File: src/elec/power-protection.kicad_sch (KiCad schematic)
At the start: 11 parts, among them J1 Conn_01x03_Pin, Q1 BSS138, Q2 BSS138, Q3 BC857, Q4 BC857

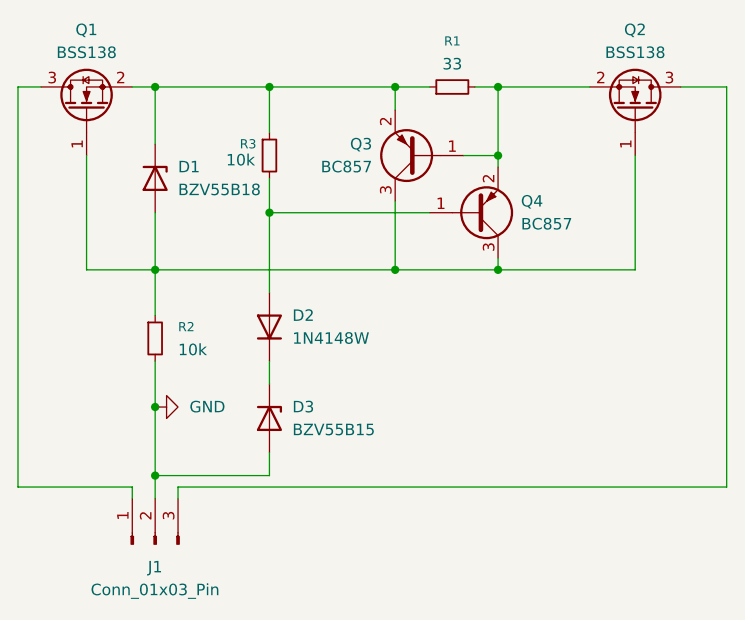
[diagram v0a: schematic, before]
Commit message: Fix: wrong MOSFET (p channel needed); README.md added
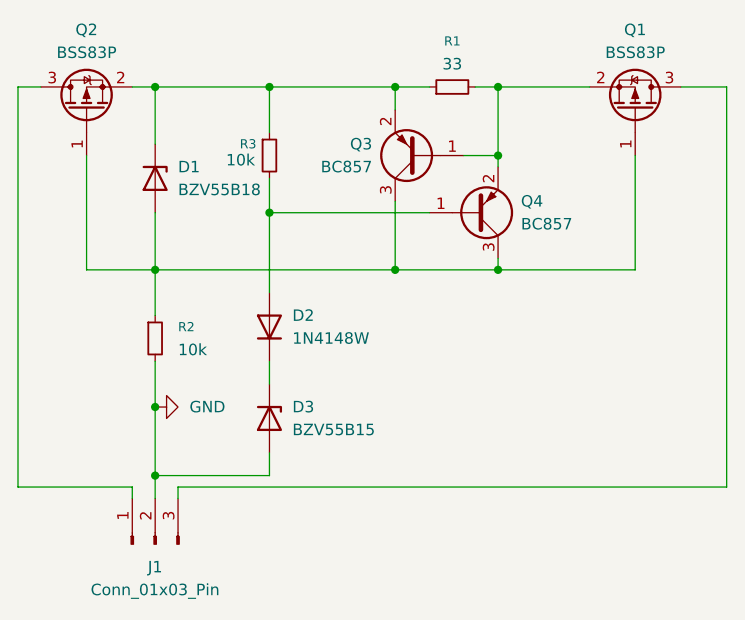
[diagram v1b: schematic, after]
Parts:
- removed Q1, Q2: BSS138, Package_TO_SOT_SMD:SOT-23, symbol Transistor_FET:BSS138
- added Q1, Q2: BSS83P, Package_TO_SOT_SMD:SOT-23, symbol Transistor_FET:BSS83P
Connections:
- net at J1.1 (Pin_1): now also Q2.3 (D)
- net at J1.3 (Pin_3): now also Q1.3 (D)
- net at Q3.1 (B), Q4.2 (E), R1.2: now also Q1.2 (S)
- net at D1.1 (K), Q3.2 (E), R1.1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: now also Q2.2 (S)
- net at D1.2 (A), Q3.3 (C), Q4.3 (C)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: now also Q1.1 (G), Q2.1 (G)
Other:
- title: (none) -> FUSE UIr
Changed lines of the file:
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@@
 	(generator_version "9.0")
 	(paper "A4")
+	(title_block
+		(title "FUSE UIr")
+		(date "2026-01-03")
+		(rev "0.2")
+	)
 	(junction
 		(at 62.23 26.67)
@@
 	)
 	(symbol
+		(lib_id "Transistor_FET:BSS83P")
+		(at 54.61 29.21 90)
+		(unit 1)
+		(exclude_from_sim no)
+		(in_bom yes)
+		(on_board yes)
+		(dnp no)
+		(property "Reference" "Q2"
+			(at 54.61 20.32 90)
+			(effects
+				(font
+					(size 1.27 1.27)
+				)
+			)
+		)
+		(property "Value" "BSS83P"
+			(at 54.61 22.86 90)
+			(effects
+				(font
+					(size 1.27 1.27)
+				)
+			)
+		)
+		(property "Footprint" "Package_TO_SOT_SMD:SOT-23"
+			(at 56.515 24.13 0)
+			(effects
+				(font
+					(size 1.27 1.27)
+					(italic yes)
+				)
+				(justify left)
+				(hide yes)
+			)
+		)
+		(property "Datasheet" "http://www.farnell.com/datasheets/1835997.pdf"
+			(at 58.42 24.13 0)
+			(effects
+				(font
+					(size 1.27 1.27)
+				)
+				(justify left)
+				(hide yes)
+			)
+		)
+		(property "Description" "-0.33A Id, -60V Vds, P-Channel MOSFET, SOT-23"
+			(at 54.61 29.21 0)
+			(effects
+				(font
+					(size 1.27 1.27)
+				)
+				(hide yes)
+			)
+		)
+		(pin "2"
+		)
+		(pin "1"
+		)
+		(pin "3"
+		)
+		(instances
+			(project "power-protection"
+				(path "/f96ba537-a636-4056-ab3e-8435b128c895"
+					(reference "Q2")
+					(unit 1)
+				)
+			)
+		)
+	)
+	(symbol
 		(lib_id "Diode:BZV55B15")
 		(at 74.93 63.5 270)
@@
 	)
 	(symbol
-		(lib_id "Transistor_FET:BSS138")
-		(at 115.57 29.21 270)
-		(mirror x)
-		(unit 1)
-		(exclude_from_sim no)
-		(in_bom yes)
-		(on_board yes)
-		(dnp no)
-		(property "Reference" "Q2"
-			(at 115.57 20.32 90)
-			(effects
-				(font
-					(size 1.27 1.27)
-				)
-			)
-		)
-		(property "Value" "BSS138"
-			(at 115.57 22.86 90)
-			(effects
-				(font
-					(size 1.27 1.27)
-				)
-			)
-		)
-		(property "Footprint" "Package_TO_SOT_SMD:SOT-23"
-			(at 113.665 24.13 0)
-			(effects
-				(font
-					(size 1.27 1.27)
-					(italic yes)
-				)
-				(justify left)
-				(hide yes)
-			)
-		)
-		(property "Datasheet" "https://www.onsemi.com/pub/Collateral/BSS138-D.PDF"
-			(at 111.76 24.13 0)
-			(effects
-				(font
-					(size 1.27 1.27)
-				)
-				(justify left)
-				(hide yes)
-			)
-		)
-		(property "Description" "50V Vds, 0.22A Id, N-Channel MOSFET, SOT-23"
-			(at 115.57 29.21 0)
-			(effects
-				(font
-					(size 1.27 1.27)
-				)
-				(hide yes)
-			)
-		)
-		(pin "2"
-		)
-		(pin "3"
-		)
-		(pin "1"
-		)
-		(instances
-			(project ""
-				(path "/f96ba537-a636-4056-ab3e-8435b128c895"
-					(reference "Q2")
-					(unit 1)
-				)
-			)
-		)
-	)
-	(symbol
 		(lib_id "Device:R_Small")
 		(at 74.93 34.29 0)
@@
 	)
 	(symbol
-		(lib_id "Transistor_FET:BSS138")
-		(at 54.61 29.21 90)
+		(lib_id "Transistor_FET:BSS83P")
+		(at 115.57 29.21 270)
+		(mirror x)
 		(unit 1)
 		(exclude_from_sim no)
@@
 		(on_board yes)
 		(dnp no)
-		(fields_autoplaced yes)
 		(property "Reference" "Q1"
-			(at 54.61 20.32 90)
-			(effects
-				(font
-					(size 1.27 1.27)
-				)
-			)
-		)
-		(property "Value" "BSS138"
-			(at 54.61 22.86 90)
+			(at 115.57 20.32 90)
+			(effects
+				(font
+					(size 1.27 1.27)
+				)
+			)
+		)
+		(property "Value" "BSS83P"
+			(at 115.57 22.86 90)
 			(effects
 				(font
@@
 		)
 		(property "Footprint" "Package_TO_SOT_SMD:SOT-23"
-			(at 56.515 24.13 0)
+			(at 113.665 24.13 0)
 			(effects
 				(font
@@
 			)
 		)
-		(property "Datasheet" "https://www.onsemi.com/pub/Collateral/BSS138-D.PDF"
-			(at 58.42 24.13 0)
-			(effects
-				(font
-					(size 1.27 1.27)
-				)
-				(justify left)
-				(hide yes)
-			)
-		)
-		(property "Description" "50V Vds, 0.22A Id, N-Channel MOSFET, SOT-23"
-			(at 54.61 29.21 0)
+		(property "Datasheet" "http://www.farnell.com/datasheets/1835997.pdf"
+			(at 111.76 24.13 0)
+			(effects
+				(font
+					(size 1.27 1.27)
+				)
+				(justify left)
+				(hide yes)
+			)
+		)
+		(property "Description" "-0.33A Id, -60V Vds, P-Channel MOSFET, SOT-23"
+			(at 115.57 29.21 0)
 			(effects
 				(font
@@
 		(pin "2"
 		)
+		(pin "1"
+		)
 		(pin "3"
 		)
-		(pin "1"
-		)
 		(instances
-			(project ""
+			(project "power-protection"
 				(path "/f96ba537-a636-4056-ab3e-8435b128c895"
 					(reference "Q1")

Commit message: started fixing
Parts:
- removed D2: 1N4148W, Diode_SMD:D_SOD-123, symbol Diode:1N4148W
- added R4: 10k, Resistor_SMD:R_0805_2012Metric, symbol Device:R_Small
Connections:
- net at D3.1 (K): now also R3.2, R4.2
- net at Q4.1 (B): now also R4.1; no longer R3.2
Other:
- moved on the sheet: D3
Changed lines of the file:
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@@
+	)
+	(junction
+		(at 62.23 68.58)
+		(diameter 0)
+		(color 0 0 0 0)
 	)
 	(junction
@@
 	)
 	(junction
-		(at 62.23 62.23)
-		(diameter 0)
-		(color 0 0 0 0)
-	)
-	(junction
-		(at 62.23 69.85)
-		(diameter 0)
-		(color 0 0 0 0)
-	)
-	(junction
 		(at 100.33 26.67)
 		(diameter 0)
@@
 	)
 	(junction
+		(at 62.23 59.69)
+		(diameter 0)
+		(color 0 0 0 0)
+	)
+	(junction
 		(at 100.33 34.29)
 		(diameter 0)
@@
 	(wire
 		(pts
-			(xy 74.93 67.31) (xy 74.93 69.85)
+			(xy 74.93 58.42) (xy 74.93 59.69)
 		)
 		(stroke
@@
 	(wire
 		(pts
+			(xy 76.2 40.64) (xy 74.93 40.64)
+		)
+		(stroke
+			(width 0)
+			(type default)
+		)
+	)
+	(wire
+		(pts
 			(xy 125.73 71.12) (xy 64.77 71.12)
 		)
@@
 	(wire
 		(pts
-			(xy 62.23 62.23) (xy 62.23 69.85)
-		)
-		(stroke
-			(width 0)
-			(type default)
-		)
-	)
-	(wire
-		(pts
 			(xy 62.23 26.67) (xy 62.23 33.02)
 		)
@@
 	(wire
 		(pts
-			(xy 62.23 69.85) (xy 74.93 69.85)
+			(xy 62.23 59.69) (xy 74.93 59.69)
 		)
 		(stroke
@@
 	(wire
 		(pts
-			(xy 74.93 40.64) (xy 74.93 49.53)
-		)
-		(stroke
-			(width 0)
-			(type default)
-		)
-	)
-	(wire
-		(pts
 			(xy 100.33 45.72) (xy 100.33 46.99)
 		)
@@
 	(wire
 		(pts
-			(xy 62.23 69.85) (xy 62.23 72.39)
-		)
-		(stroke
-			(width 0)
-			(type default)
-		)
-	)
-	(wire
-		(pts
-			(xy 92.71 40.64) (xy 74.93 40.64)
+			(xy 62.23 59.69) (xy 62.23 68.58)
+		)
+		(stroke
+			(width 0)
+			(type default)
+		)
+	)
+	(wire
+		(pts
+			(xy 92.71 40.64) (xy 81.28 40.64)
 		)
 		(stroke
@@
 	(wire
 		(pts
-			(xy 62.23 57.15) (xy 62.23 62.23)
+			(xy 62.23 57.15) (xy 62.23 59.69)
 		)
 		(stroke
@@
 	(wire
 		(pts
+			(xy 62.23 68.58) (xy 62.23 72.39)
+		)
+		(stroke
+			(width 0)
+			(type default)
+		)
+	)
+	(wire
+		(pts
 			(xy 100.33 34.29) (xy 100.33 35.56)
 		)
@@
 	(wire
 		(pts
-			(xy 74.93 57.15) (xy 74.93 59.69)
+			(xy 74.93 40.64) (xy 74.93 50.8)
 		)
 		(stroke
@@
 	(symbol
 		(lib_id "Diode:BZV55B15")
-		(at 74.93 63.5 270)
+		(at 74.93 54.61 270)
 		(unit 1)
 		(exclude_from_sim no)
@@
 		(fields_autoplaced yes)
 		(property "Reference" "D3"
-			(at 77.47 62.2299 90)
+			(at 77.47 53.3399 90)
 			(effects
 				(font
@@
 		)
 		(property "Value" "BZV55B15"
-			(at 77.47 64.7699 90)
+			(at 77.47 55.8799 90)
 			(effects
 				(font
@@
 		)
 		(property "Footprint" "Diode_SMD:D_MiniMELF"
-			(at 70.485 63.5 0)
+			(at 70.485 54.61 0)
 			(effects
 				(font
@@
 		)
 		(property "Datasheet" "https://assets.nexperia.com/documents/data-sheet/BZV55_SER.pdf"
-			(at 74.93 63.5 0)
+			(at 74.93 54.61 0)
 			(effects
 				(font
@@
 		)
 		(property "Description" "15V, 500mW, 2%, Zener diode, MiniMELF"
-			(at 74.93 63.5 0)
+			(at 74.93 54.61 0)
 			(effects
 				(font
@@
 				(path "/f96ba537-a636-4056-ab3e-8435b128c895"
 					(reference "D3")
-					(unit 1)
-				)
-			)
-		)
-	)
-	(symbol
-		(lib_id "Diode:1N4148W")
-		(at 74.93 53.34 90)
-		(unit 1)
-		(exclude_from_sim no)
-		(in_bom yes)
-		(on_board yes)
-		(dnp no)
-		(fields_autoplaced yes)
-		(property "Reference" "D2"
-			(at 77.47 52.0699 90)
-			(effects
-				(font
-					(size 1.27 1.27)
-				)
-				(justify right)
-			)
-		)
-		(property "Value" "1N4148W"
-			(at 77.47 54.6099 90)
-			(effects
-				(font
-					(size 1.27 1.27)
-				)
-				(justify right)
-			)
-		)
-		(property "Footprint" "Diode_SMD:D_SOD-123"
-			(at 79.375 53.34 0)
-			(effects
-				(font
-					(size 1.27 1.27)
-				)
-				(hide yes)
-			)
-		)
-		(property "Datasheet" "https://www.vishay.com/docs/85748/1n4148w.pdf"
-			(at 74.93 53.34 0)
-			(effects
-				(font
-					(size 1.27 1.27)
-				)
-				(hide yes)
-			)
-		)
-		(property "Description" "75V 0.15A Fast Switching Diode, SOD-123"
-			(at 74.93 53.34 0)
-			(effects
-				(font
-					(size 1.27 1.27)
-				)
-				(hide yes)
-			)
-		)
-		(property "Sim.Device" "D"
-			(at 74.93 53.34 0)
-			(effects
-				(font
-					(size 1.27 1.27)
-				)
-				(hide yes)
-			)
-		)
-		(property "Sim.Pins" "1=K 2=A"
-			(at 74.93 53.34 0)
-			(effects
-				(font
-					(size 1.27 1.27)
-				)
-				(hide yes)
-			)
-		)
-		(pin "2"
-		)
-		(pin "1"
-		)
-		(instances
-			(project ""
-				(path "/f96ba537-a636-4056-ab3e-8435b128c895"
-					(reference "D2")
 					(unit 1)
 				)
@@
 	(symbol
 		(lib_id "power:GND")
-		(at 62.23 62.23 90)
+		(at 62.23 68.58 90)
 		(unit 1)
 		(exclude_from_sim no)
@@
 		(fields_autoplaced yes)
 		(property "Reference" "#PWR01"
-			(at 68.58 62.23 0)
+			(at 68.58 68.58 0)
 			(effects
 				(font
@@
 		)
 		(property "Value" "GND"
-			(at 66.04 62.2299 90)
+			(at 66.04 68.5799 90)
 			(effects
 				(font
@@
 		)
 		(property "Footprint" ""
-			(at 62.23 62.23 0)
+			(at 62.23 68.58 0)
 			(effects
 				(font
@@
 		)
 		(property "Datasheet" ""
-			(at 62.23 62.23 0)
+			(at 62.23 68.58 0)
 			(effects
 				(font
@@
 		)
 		(property "Description" "Power symbol creates a global label with name \"GND\" , ground"
-			(at 62.23 62.23 0)
+			(at 62.23 68.58 0)
 			(effects
 				(font
@@
 					(unit 1)
 				)
+			)
+		)
+	)
+	(symbol
+		(lib_id "Device:R_Small")
+		(at 78.74 40.64 270)
+		(unit 1)
+		(exclude_from_sim no)
+		(in_bom yes)
+		(on_board yes)
+		(dnp no)
+		(property "Reference" "R4"
+			(at 80.01 37.338 0)
+			(effects
+				(font
+					(size 1.016 1.016)
+				)
+				(justify left)
+			)
+		)
+		(property "Value" "10k"
+			(at 78.232 35.814 0)
+			(effects
+				(font
+					(size 1.27 1.27)
+				)
+				(justify left)
+			)
+		)
+		(property "Footprint" "Resistor_SMD:R_0805_2012Metric"
+			(at 78.74 40.64 0)
+			(effects
+				(font
+					(size 1.27 1.27)
+				)
+				(hide yes)
+			)
+		)
+		(property "Datasheet" "~"
+			(at 78.74 40.64 0)
+			(effects
+				(font
+					(size 1.27 1.27)
+				)
+				(hide yes)
+			)
+		)
+		(property "Description" "Resistor, small symbol"
+			(at 78.74 40.64 0)
+			(effects
+				(font
+					(size 1.27 1.27)
+				)
+				(hide yes)
+			)
+		)
+		(pin "1"
+		)
+		(pin "2"
+		)
+		(instances
+			(project "power-protection"
+				(path "/f96ba537-a636-4056-ab3e-8435b128c895"
+					(reference "R4")
+					(unit 1)
+				)
